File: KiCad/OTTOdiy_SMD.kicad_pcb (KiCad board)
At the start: 4 copper layers, 297 x 91 mm, 438 parts, among them CN201 1x4 MALE Molex PicoBlade, CN202 1x4 MALE Molex PicoBlade, J1 Conn_ARM_JTAG_SWD_10, J2 Conn_02x04, J201 Raspberry Pi Connector, J202 Conn_02x04, J203 Conn_02x05, J204 Conn_02x05, J205 Conn_02x04, J206 Conn_02x06, J207 Conn_02x03, Q1 AO4485, SW1 ALPS SKHH OR SKPF, SW10 ALPS SKHH OR SKPF, SW11 ALPS SKHH OR SKPF, SW12 ALPS SKHH OR SKPF, SW13 ALPS SKHH OR SKPF, SW14 ALPS SKHH OR SKPF, SW15 ALPS SKHH OR SKPF, SW16 ALPS SKHH OR SKPF, SW17 ALPS SKHH OR SKPF, SW18 ALPS SKHH OR SKPF, SW19 ALPS SKHH OR SKPF, SW2 ALPS SKHH OR SKPF, SW20 ALPS SKHH OR SKPF, SW201 5.2x5.2x1.5mm, SW202 SW_DIP_x02, SW203 6x6x5.85mm (RA), SW21 ALPS SKHH OR SKPF, SW22 ALPS SKHH OR SKPF, SW23 ALPS SKHH OR SKPF, SW24 ALPS SKHH OR SKPF, SW25 ALPS SKHH OR SKPF, SW26 ALPS SKHH OR SKPF, SW27 6x6x13mm, SW28 6x6x13mm, SW29 6x6x13mm, SW3 ALPS SKHH OR SKPF, SW30 6x6x13mm, SW31 6x6x13mm, SW32 6x6x13mm, SW33 6x6x13mm, SW34 6x6x13mm, SW35 6x6x13mm, SW36 6x6x13mm, SW37 6x6x13mm, SW38 6x6x13mm, SW39 6x6x13mm, SW4 ALPS SKHH OR SKPF, SW40 6x6x13mm, SW41 6x6x13mm, SW42 6x6x13mm, SW43 6x6x13mm, SW44 6x6x13mm, SW45 6x6x13mm, SW46 6x6x13mm, SW47 6x6x13mm, SW48 SW_DIP_x02, SW49 SW_SP3T (DP3T Parallel), SW5 ALPS SKHH OR SKPF, SW6 ALPS SKHH OR SKPF, SW7 ALPS SKHH OR SKPF, SW8 ALPS SKHH OR SKPF, SW9 ALPS SKHH OR SKPF, U1 SN74LV1T125_SOT-23_A, U2 TPS22918_SOT23-6_A, U202 STM32F407VGTx, U204 USB6B1, U205 SN74HC14, U206 H11L1S, U207 WM8731, U208 TPS79533, U3 LTC3112_TSSOP20_A, U4 TLV62568_SOT-23-5_A, U5 TPS22918_SOT23-6_A, Y201 25MHz, Y202 32.768kHz, Y203 12.288MHz

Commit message: Add and route 7 extra buttons/LEDs
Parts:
- added C100: 100nF, Capacitor_SMD:C_0805_2012Metric_Pad1.15x1.40mm_HandSolder, B.Cu at (259.0, 111.8)
- added C101: 100nF, Capacitor_SMD:C_0805_2012Metric_Pad1.15x1.40mm_HandSolder, B.Cu at (271.0, 111.8)
- added C102: 100nF, Capacitor_SMD:C_0805_2012Metric_Pad1.15x1.40mm_HandSolder, B.Cu at (283.0, 111.8)
- added C103: 100nF, Capacitor_SMD:C_0805_2012Metric_Pad1.15x1.40mm_HandSolder, B.Cu at (295.0, 111.8)
- added C104: 100nF, Capacitor_SMD:C_0805_2012Metric_Pad1.15x1.40mm_HandSolder, B.Cu at (313.0, 111.8)
- added C105: 100nF, Capacitor_SMD:C_0805_2012Metric_Pad1.15x1.40mm_HandSolder, B.Cu at (325.0, 111.8)
- added C99: 100nF, Capacitor_SMD:C_0805_2012Metric_Pad1.15x1.40mm_HandSolder, B.Cu at (247.0, 111.8)
- added D58: SM4007PL, Diode_SMD:D_SOD-123F, B.Cu at (254.5, 119.2)
- added D59: SM4007PL, Diode_SMD:D_SOD-123F, B.Cu at (266.5, 119.2)
- added D60: SM4007PL, Diode_SMD:D_SOD-123F, B.Cu at (278.5, 119.2)
- added D61: SM4007PL, Diode_SMD:D_SOD-123F, B.Cu at (290.5, 119.2)
- added D62: SM4007PL, Diode_SMD:D_SOD-123F, B.Cu at (302.5, 119.2)
- added D63: SM4007PL, Diode_SMD:D_SOD-123F, B.Cu at (320.5, 119.2)
- added D64: SM4007PL, Diode_SMD:D_SOD-123F, B.Cu at (332.5, 119.2)
- added LED48: WS2812D-5, OTTO_Footprints_Lib:LED_D5.0mm-4, F.Cu at (249.5, 114.2)
- added LED49: WS2812D-5, OTTO_Footprints_Lib:LED_D5.0mm-4, F.Cu at (261.5, 114.2)
- added LED50: WS2812D-5, OTTO_Footprints_Lib:LED_D5.0mm-4, F.Cu at (273.5, 114.2)
- added LED51: WS2812D-5, OTTO_Footprints_Lib:LED_D5.0mm-4, F.Cu at (285.5, 114.2)
- added LED52: WS2812D-5, OTTO_Footprints_Lib:LED_D5.0mm-4, F.Cu at (297.5, 114.2)
- added LED53: WS2812D-5, OTTO_Footprints_Lib:LED_D5.0mm-4, F.Cu at (315.5, 114.2)
- added LED54: WS2812D-5, OTTO_Footprints_Lib:LED_D5.0mm-4, F.Cu at (327.5, 114.2)
- added SW50: 6x6x13mm, OTTO_Footprints_Lib:6x6mm_Switch, F.Cu at (254.0, 118.8)
- added SW51: 6x6x13mm, OTTO_Footprints_Lib:6x6mm_Switch, F.Cu at (266.0, 118.8)
- added SW52: 6x6x13mm, OTTO_Footprints_Lib:6x6mm_Switch, F.Cu at (278.0, 118.8)
- added SW53: 6x6x13mm, OTTO_Footprints_Lib:6x6mm_Switch, F.Cu at (290.0, 118.8)
- added SW54: 6x6x13mm, OTTO_Footprints_Lib:6x6mm_Switch, F.Cu at (302.0, 118.8)
- added SW55: 6x6x13mm, OTTO_Footprints_Lib:6x6mm_Switch, F.Cu at (320.0, 118.8)
- added SW56: 6x6x13mm, OTTO_Footprints_Lib:6x6mm_Switch, F.Cu at (332.0, 118.8)
- moved H206 12.3 mm to (242.0, 98.0)
- moved C34 6.00 mm to (247.0, 135.8)
- moved C35 6.00 mm to (259.0, 135.8)
- moved C36 6.00 mm to (271.0, 135.8)
- moved C37 6.00 mm to (283.0, 135.8)
- moved C38 6.00 mm to (295.0, 135.8)
- moved C39 6.00 mm to (313.0, 135.8)
- moved C40 6.00 mm to (325.0, 135.8)
- moved C41 6.00 mm to (247.0, 123.8)
- moved C42 6.00 mm to (259.0, 123.8)
- moved C43 6.00 mm to (271.0, 123.8)
- moved C44 6.00 mm to (283.0, 123.8)
- moved C45 6.00 mm to (295.0, 123.8)
- moved C46 6.00 mm to (313.0, 123.8)
- moved C47 6.00 mm to (325.0, 123.8)
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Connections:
- LED47 pad 1: /MCU/LEDS/LED_OUT -> /MCU/LEDS/LED_CONN3
- U202 pad 78: Net-(U202-Pad78) -> /MCU/COL_8
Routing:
- net /MCU/COL_8: track 0.00 -> 133.4 mm
- net /MCU/LEDS/LED_CONN3: track 0.00 -> 102.4 mm
- net /MCU/LEDS/LED_CONN2: track 0.00 -> 92.6 mm
- net /MCU/ROW_4: track 484.1 -> 435.7 mm, vias 6 -> 8
- net /MCU/ROW_3: track 315.1 -> 357.1 mm, vias 6 -> 7
- net /MCU/COL_6: track 146.5 -> 117.5 mm
- net +5V_LEDS: track 173.0 -> 199.6 mm
- net GND: track 341.5 -> 367.4 mm
- net /MCU/ROW_1: track 432.4 -> 407.5 mm, vias 6 -> 7
- net /MCU/ROW_6: track 413.2 -> 388.9 mm, vias 7 -> 9
- net /MCU/ROW_7: track 389.1 -> 410.0 mm, vias 7 -> 8
- net /MCU/COL_2: track 144.3 -> 161.0 mm, vias 0 -> 1
- net Net-(LED52-Pad1): track 0.00 -> 16.4 mm
- net /MCU/COL_3: track 141.7 -> 156.9 mm, vias 0 -> 2
- net /MCU/COL_4: track 151.5 -> 166.3 mm, vias 0 -> 1
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
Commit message: [wip] routing MCU expansion headers
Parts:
- moved C53 0.40 mm to (80.7, 140.8)
- moved C222 0.40 mm to (79.8, 143.6)
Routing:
- net /MCU/COL_5: track 152.7 -> 347.1 mm
- net /MCU/LEDS/LED_CONN1: track 0.00 -> 173.9 mm
- net /MCU/COL_6: track 117.5 -> 265.5 mm
- net /MCU/COL_8: track 133.4 -> 277.9 mm
- net /MCU/COL_7: track 0.00 -> 101.3 mm
- net /MCU/ROW_1: track 407.5 -> 477.1 mm, vias 7 -> 8
- net /MCU/ROW_2: track 360.2 -> 421.7 mm, vias 8 -> 9
- net /MCU/COL_1: track 144.3 -> 180.9 mm
- net /MCU/GATE_IO_1: track 0.00 -> 36.4 mm, vias 0 -> 1
- net /MCU/CV_ADC_1: track 0.00 -> 35.3 mm, vias 0 -> 1
- net /MCU/ENC_A_1: track 2.61 -> 36.2 mm, vias 0 -> 1
- net /MCU/GATE_IO_2: track 0.00 -> 33.4 mm, vias 0 -> 1
- net /MCU/CV_ADC_2: track 0.00 -> 32.5 mm, vias 0 -> 1
- net /MCU/CV_DAC_1: track 0.00 -> 31.4 mm, vias 0 -> 1
- net /MCU/CV_DAC_2: track 0.00 -> 31.3 mm, vias 0 -> 1
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
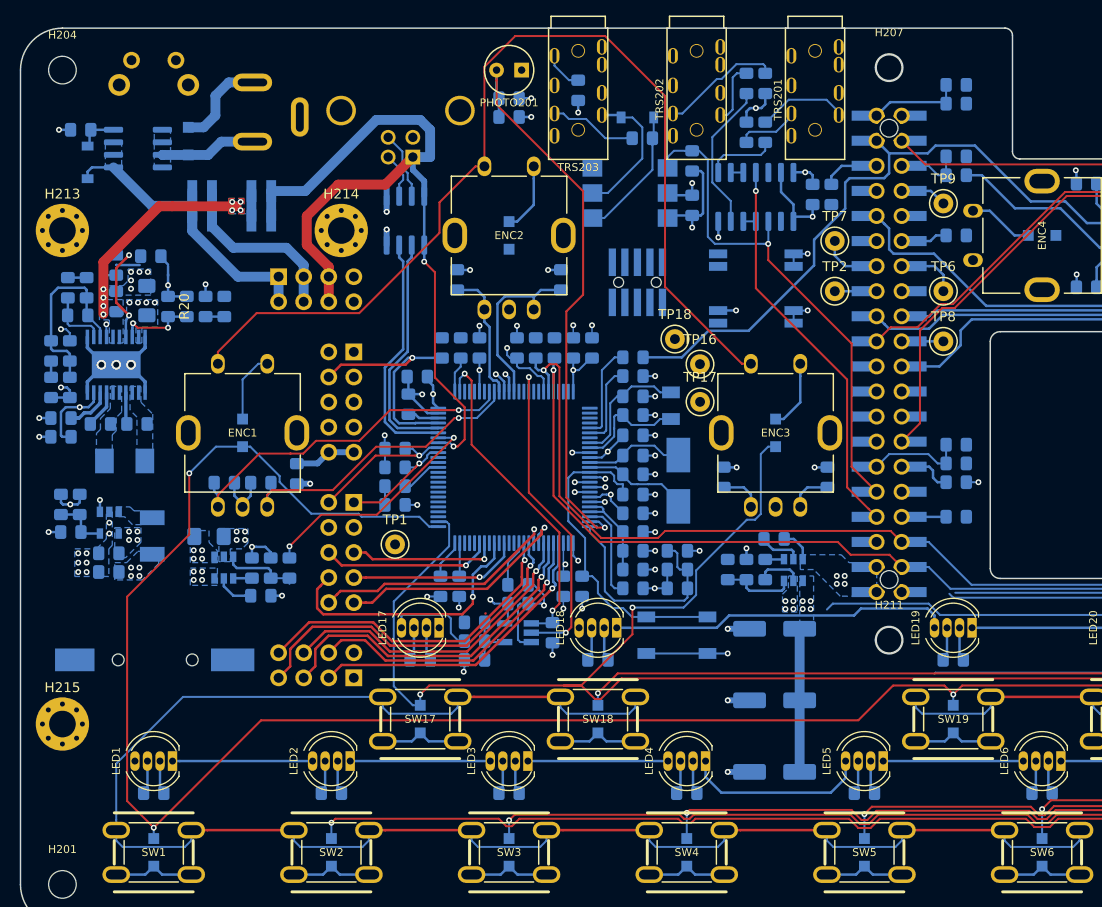
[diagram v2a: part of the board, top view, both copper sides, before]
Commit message: More MCU connections routed
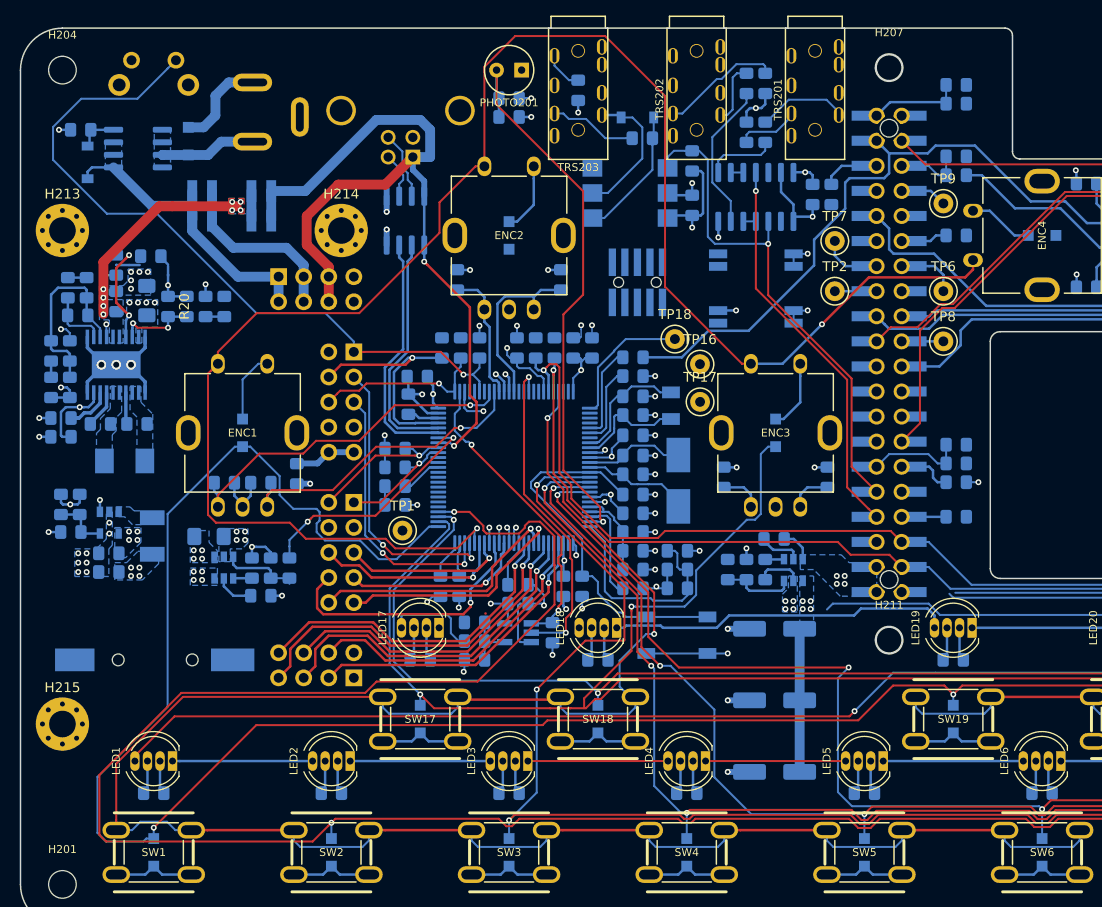
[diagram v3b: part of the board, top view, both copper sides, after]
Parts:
- moved TP1 1.59 mm to (79.2, 156.4)
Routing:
- net /MCU/ROW_4: track 435.7 -> 540.7 mm, vias 8 -> 9
- net /MCU/LEDS/LED_CONN1: track 173.9 -> 258.9 mm, vias 0 -> 1
- net /MCU/ROW_8: track 426.2 -> 502.3 mm, vias 9 -> 10
- net /MCU/COL_7: track 101.3 -> 175.5 mm, vias 0 -> 2
- net PWR_BUTTON: track 4.20 -> 75.5 mm
- net /MCU/ROW_7: track 410.0 -> 465.8 mm, vias 8 -> 9
- net /MCU/ROW_5: track 454.1 -> 503.0 mm, vias 7 -> 8
- net /MCU/ROW_6: track 388.9 -> 431.4 mm, vias 9 -> 10
- net /MCU/ROW_3: track 357.1 -> 397.7 mm, vias 7 -> 8
- net /MCU/COL_1: track 180.9 -> 217.9 mm, vias 0 -> 2
- net /MCU/PROG_UART_TX: track 0.00 -> 29.4 mm, vias 0 -> 2
- net /MCU/PROG_UART_RX: track 0.00 -> 27.4 mm, vias 0 -> 2
- net /ICP_SWCLK: track 3.65 -> 17.5 mm, vias 0 -> 1
- net (F427)_SAI1_MCLK_A: track 0.00 -> 13.8 mm
- net /MCU/ROW_1: track 477.1 -> 488.0 mm, vias 8 -> 7
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
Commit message: Even more MCU connections routed
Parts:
- moved TP18 1.00 mm to (105.8, 137.1)
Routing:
- net /MCU/COL_4: track 168.0 -> 352.5 mm, vias 2 -> 3
- net MIDI_OUT: track 43.6 -> 205.6 mm
- net MIDI_IN: track 53.9 -> 212.3 mm, vias 2 -> 1
- net /MCU/ROW_4: track 540.7 -> 688.7 mm, vias 9 -> 10
- net /AUDIO/I2S_BCLK*: track 0.00 -> 136.2 mm
- net /MCU/COL_3: track 158.6 -> 283.4 mm, vias 3 -> 4
- net /AUDIO/I2S_DOUT*: track 0.00 -> 92.6 mm, vias 0 -> 1
- net /MCU/ENC_B_4: track 4.30 -> 88.7 mm, vias 0 -> 3
- net AMP_ENABLE: track 5.58 -> 89.3 mm, vias 0 -> 1
- net /MCU/ENC_A_4: track 4.30 -> 86.4 mm, vias 0 -> 3
- net PI_PWR_EN: track 0.00 -> 77.4 mm, vias 0 -> 3
- net /PWM1_GPIO13_RASPI: track 3.32 -> 76.9 mm, vias 0 -> 1
- net /MCU/COL_2: track 161.0 -> 227.9 mm, vias 1 -> 3
- net /MCU/COL_8: track 281.7 -> 347.3 mm, vias 1 -> 2
- net /MCU/COL_6: track 267.0 -> 330.8 mm, vias 1 -> 2
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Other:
- outline, holes or cut-outs redrawn

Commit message: Routed everything but power
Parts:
- moved TP17 29.3 mm to (81.7, 133.7), turned to 90 degrees
- moved TP16 29.0 mm to (81.7, 130.6), turned to 90 degrees
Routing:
- net /MCU/LEDS/LED_OUT: track 0.00 -> 375.6 mm
- net /MCU/BRIGHTNESS: track 4.85 -> 100.2 mm, vias 0 -> 2
- net Net-(MK201-Pad2): track 0.00 -> 89.1 mm, vias 0 -> 1
- net /MCU/ROW_7: track 468.2 -> 528.1 mm, vias 9 -> 12
- net /MCU/BOOT1: track 4.96 -> 54.1 mm, vias 0 -> 2
- net /ICP_SWDIO: track 48.2 -> 97.0 mm, vias 3 -> 5
- net /MCU/COL_7: track 113.7 -> 155.0 mm, vias 2 -> 3
- net Net-(R16-Pad1): track 9.35 -> 42.8 mm, vias 1 -> 3
- net /ICP_RST: track 72.1 -> 102.3 mm, vias 4 -> 5
- net /MCU/SPI_SCLK_MCU: track 0.00 -> 21.2 mm, vias 0 -> 1
- net /MCU/SPI_MISO_MCU: track 0.00 -> 17.9 mm, vias 0 -> 1
- net /MCU/ROW_5: track 505.5 -> 498.6 mm
- net /MCU/ROW_3: track 397.5 -> 403.3 mm
- net /MCU/ROW_2: track 420.8 -> 426.6 mm
- net /MCU/ROW_1: track 495.9 -> 500.5 mm
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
